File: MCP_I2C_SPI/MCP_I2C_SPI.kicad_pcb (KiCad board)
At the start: 2 copper layers, 46 parts, among them J1 GPA, J10 VCC, J11 GND, J12 I2C, J13 Interrupt0, J14 A2, J15 A1, J16 A0, J17 SDA, J18 SCK, J19 INTA, J2 GPB, J20 INTB, J21 V0, J22 Ext, J23 SPI, J24 InterruptS, J25 A2, J27 GPB, J28 GPA, J29 A1, J3 Data, J31 A0, J32 INTA, J33 INTB, J4 Control, J5 Zlacze_LCD, J6 VSS, J7 K, J8 VDD, J9 A, U1 MCP23017_SP, U2 MCP23017_SP

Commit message: Płytka MCP in progress
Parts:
- moved J27 120.3 mm to (135.0, 122.6), turned to 180 degrees
- moved J23 118.1 mm to (143.4, 51.0)
- moved J28 114.2 mm to (135.0, 98.2), turned to 180 degrees
- moved J24 96.1 mm to (143.4, 65.5)
- moved C2 93.5 mm to (156.5, 98.1), turned to -90 degrees
- moved R11 92.8 mm to (155.3, 55.2)
- moved R12 92.1 mm to (155.3, 64.3)
- moved R7 92.0 mm to (155.3, 68.9)
- moved R10 91.9 mm to (155.3, 59.8)
- moved J32 83.0 mm to (173.9, 53.6)
- moved J33 83.0 mm to (178.5, 53.6)
- moved U2 71.1 mm to (161.4, 78.7)
- moved J25 70.5 mm to (174.1, 65.9)
- moved J29 70.5 mm to (178.7, 65.9)
- moved J31 70.5 mm to (183.3, 65.9)
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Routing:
- net GND: track 0.00 -> 217.4 mm
- net +5V: track 2.54 -> 164.6 mm
- net Net-(J5-Pin_15): track 0.00 -> 110.7 mm, vias 0 -> 1
- net SDA: track 0.00 -> 105.1 mm, vias 0 -> 1
- net Net-(J5-Pin_16): track 0.00 -> 103.8 mm, vias 0 -> 1
- net Net-(J2-Pin_1): track 0.00 -> 102.3 mm
- net Net-(J2-Pin_2): track 0.00 -> 97.6 mm
- net Net-(J2-Pin_3): track 0.00 -> 92.8 mm
- net Net-(J5-Pin_2): track 0.00 -> 90.9 mm
- net Net-(J2-Pin_4): track 0.00 -> 88.3 mm
- net SCL: track 0.00 -> 84.3 mm, vias 0 -> 1
- net Net-(J2-Pin_5): track 0.00 -> 83.7 mm
- net INTB0: track 0.00 -> 80.1 mm, vias 0 -> 1
- net Net-(J2-Pin_6): track 0.00 -> 78.5 mm
- net INTA0: track 0.00 -> 72.7 mm, vias 0 -> 1
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
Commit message: Płytka MCP_I2C_SPIv1 gotowa
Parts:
- moved J21 57.7 mm to (165.2, 108.5)
- moved J22 57.7 mm to (171.2, 113.5)
- moved RV1 57.7 mm to (181.9, 112.7)
- moved J5 20.7 mm to (58.3, 112.4)
- moved J11 20.7 mm to (83.9, 44.9)
- moved J13 20.7 mm to (97.9, 44.9)
- moved J14 20.7 mm to (122.9, 46.6)
- moved J15 20.7 mm to (128.4, 46.6)
- moved J16 20.7 mm to (133.9, 46.6)
- moved J24 20.7 mm to (142.3, 44.9)
- moved J25 20.7 mm to (173.0, 45.2)
- moved J29 20.7 mm to (177.6, 45.2)
- moved J31 20.7 mm to (182.2, 45.2)
- moved R5 20.7 mm to (104.0, 45.4)
- moved J9 20.7 mm to (62.9, 30.0)
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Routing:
- net GND: track 217.4 -> 391.7 mm
- net +5V: track 164.6 -> 319.2 mm
- net Net-(J27-Pin_1): track 10.3 -> 102.3 mm
- net Net-(J27-Pin_2): track 9.72 -> 97.6 mm
- net Net-(J27-Pin_3): track 10.3 -> 92.8 mm
- net Net-(J27-Pin_6): track 0.00 -> 78.5 mm
- net Net-(J27-Pin_4): track 10.5 -> 88.3 mm
- net Net-(J27-Pin_5): track 11.3 -> 84.5 mm
- net Net-(J27-Pin_7): track 0.00 -> 72.6 mm
- net CS: track 0.00 -> 70.2 mm
- net SCK: track 0.00 -> 69.6 mm
- net SI: track 0.00 -> 69.3 mm
- net SO: track 0.00 -> 69.0 mm
- net Net-(J27-Pin_8): track 0.00 -> 62.4 mm
- net Net-(J21-Pin_2): track 51.0 -> 105.9 mm
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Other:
- board outline added: 136 x 95 mm
- board text added: "0"
- board text added: "1"
- board text added: "2x16 LCD DISPLAY"
- board text added: "4x20 LCD DISPLAY"
- board text added: "CS"
- board text added: "D0"
- board text added: "D7"
- board text added: "E"
- board text added: "INTA"
- board text added: "INTB"
- board text added: "PA0"
- board text added: "PA7"
- board text added: "PB0"
- board text added: "PB7"
- board text added: "RESET"
- board text added: "RS"
- board text added: "RW"
- board text added: "SCK"
- board text added: "SCL"
- board text added: "SDA"
- board text added: "SI"
- board text added: "SO"

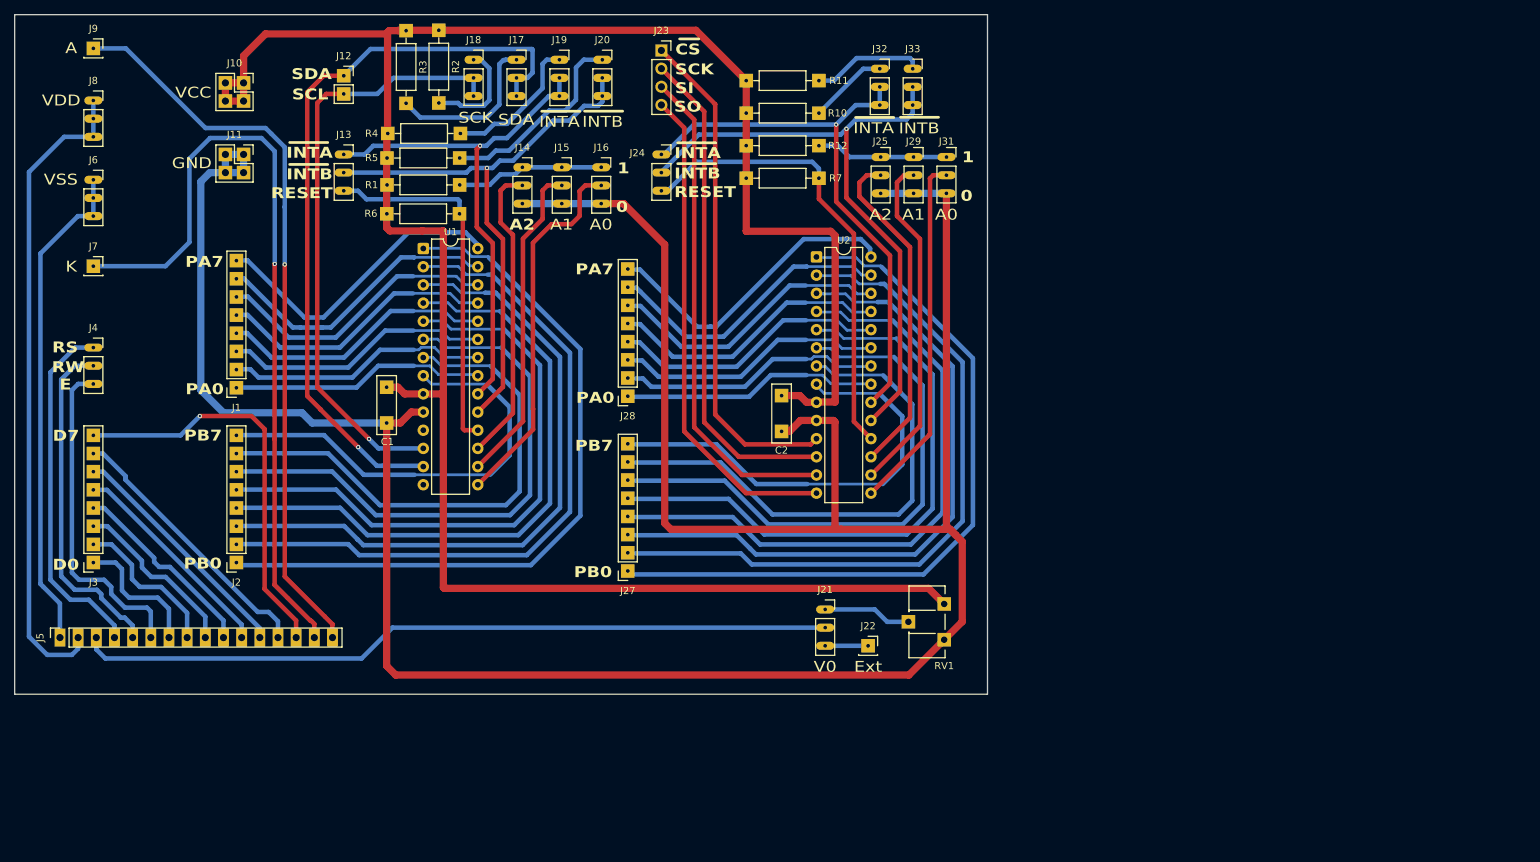
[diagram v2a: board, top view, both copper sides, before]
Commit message: Poprawki płytki MCP_I2C_SPI V1
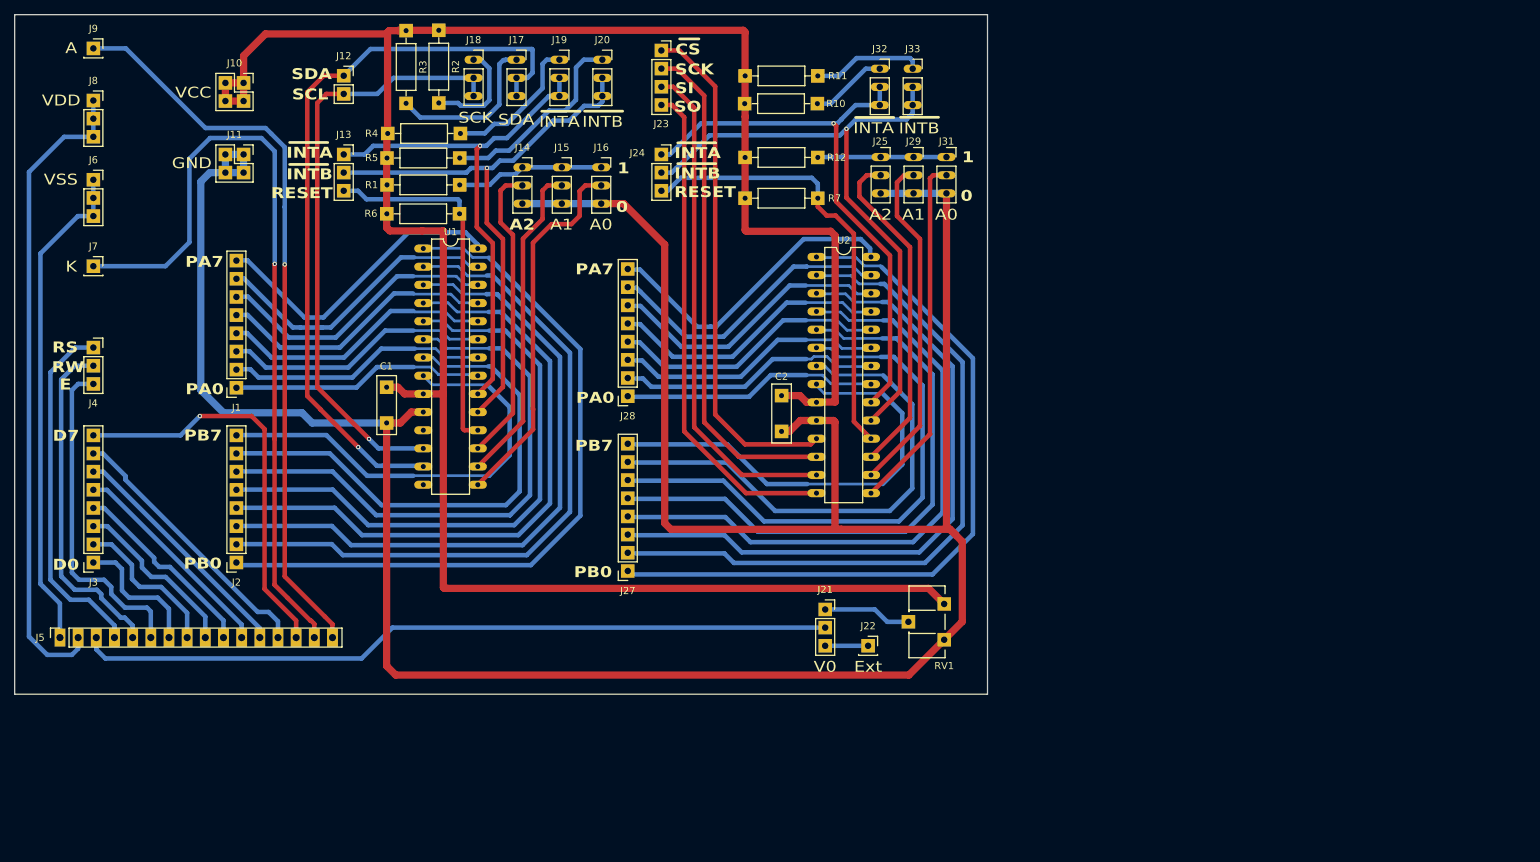
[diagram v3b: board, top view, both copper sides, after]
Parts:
- moved R7 2.80 mm to (154.1, 51.0)
- moved R12 1.65 mm to (154.1, 45.3)
- moved R10 1.34 mm to (154.0, 37.8)
- moved R11 0.68 mm to (154.1, 33.9)
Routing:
- net +5V: track 319.2 -> 323.1 mm
- net RESETS: track 64.9 -> 62.4 mm
- net CS: track 70.2 -> 71.7 mm
- net Net-(J27-Pin_7): track 72.6 -> 71.2 mm
- net SCK: track 69.6 -> 70.9 mm
- net SI: track 69.3 -> 70.3 mm
- net Net-(J27-Pin_6): track 78.5 -> 77.6 mm
- net SO: track 69.0 -> 69.9 mm
- net Net-(J27-Pin_1): track 102.3 -> 103.0 mm
- net Net-(J27-Pin_5): track 84.5 -> 83.8 mm
- net Net-(J25-Pin_1): track 18.5 -> 18.0 mm

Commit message: I2C_SPI_PCB_V2
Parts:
- moved C2 12.6 mm to (146.5, 78.6)
- moved J27 12.6 mm to (125.0, 103.1)
- moved J28 12.6 mm to (125.0, 78.6)
- moved U2 12.6 mm to (151.4, 59.2)
- moved C1 10.3 mm to (93.6, 77.4)
- moved U1 10.3 mm to (98.7, 58.0)
- moved J2 4.98 mm to (78.0, 101.9)
- moved J1 4.98 mm to (78.0, 77.5)
- moved J10 3.39 mm to (80.5, 34.9)
- moved J11 3.39 mm to (80.5, 44.9)
- moved J3 1.94 mm to (61.0, 101.9)
- moved J4 1.89 mm to (61.0, 71.9)
- moved J6 1.89 mm to (61.0, 48.4)
- moved J7 1.89 mm to (61.0, 60.5)
- moved J8 1.89 mm to (61.0, 37.3)
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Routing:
- net Net-(J5-Pin_15): track 110.7 -> 86.6 mm
- net Net-(J3-Pin_7): track 38.1 -> 57.2 mm, vias 0 -> 1
- net Net-(J3-Pin_6): track 33.6 -> 50.5 mm, vias 0 -> 1
- net GND: track 391.7 -> 408.4 mm, vias 0 -> 1
- net +5V: track 323.1 -> 311.0 mm
- net Net-(J1-Pin_8): track 43.2 -> 31.2 mm
- net Net-(J1-Pin_7): track 41.2 -> 30.1 mm
- net Net-(J1-Pin_6): track 40.1 -> 30.0 mm
- net Net-(J1-Pin_5): track 39.3 -> 30.2 mm
- net RESET0: track 51.0 -> 60.0 mm
- net Net-(J1-Pin_4): track 38.4 -> 30.2 mm
- net Net-(J1-Pin_3): track 37.3 -> 30.1 mm
- net Net-(J1-Pin_2): track 36.4 -> 30.1 mm
- net Net-(J31-Pin_2): track 49.9 -> 55.7 mm
- net Net-(J2-Pin_3): track 93.0 -> 87.6 mm
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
